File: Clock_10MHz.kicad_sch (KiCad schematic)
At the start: 8 parts, among them U3 74LV8154, U4 74LS151, X1 ASCO

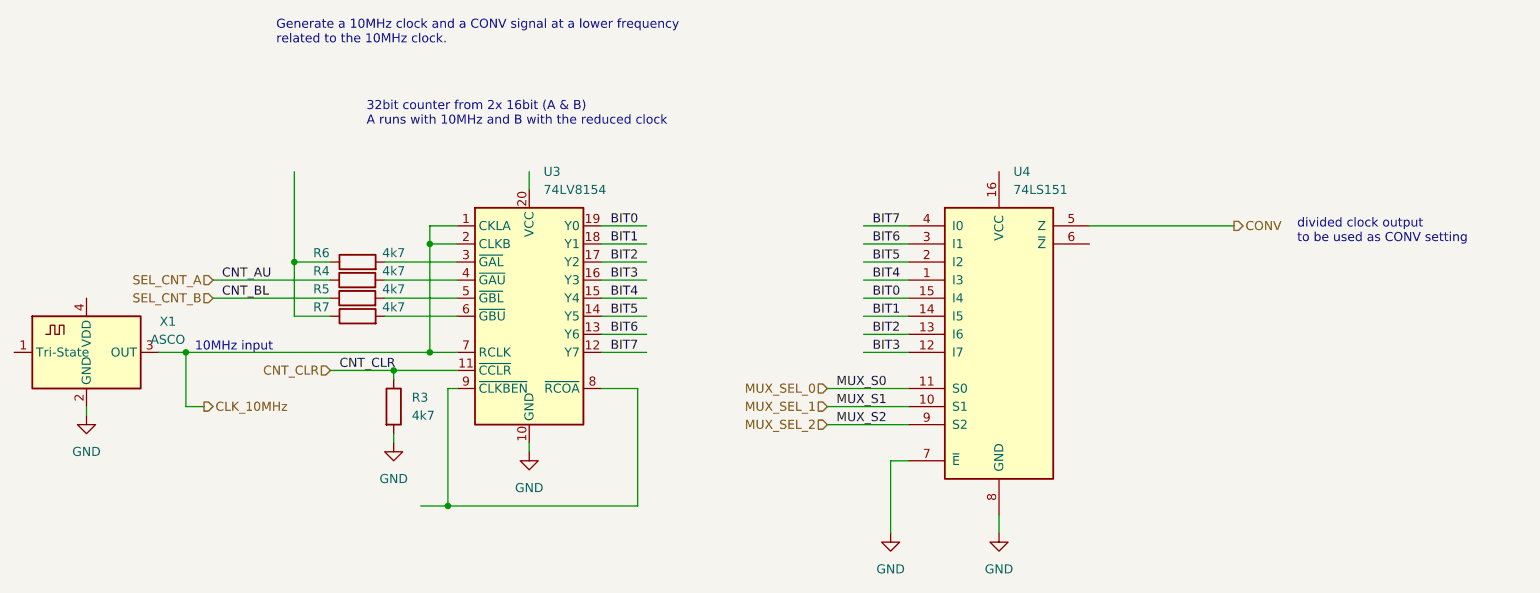
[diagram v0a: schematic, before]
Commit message: connected the ICs to 5V digital power
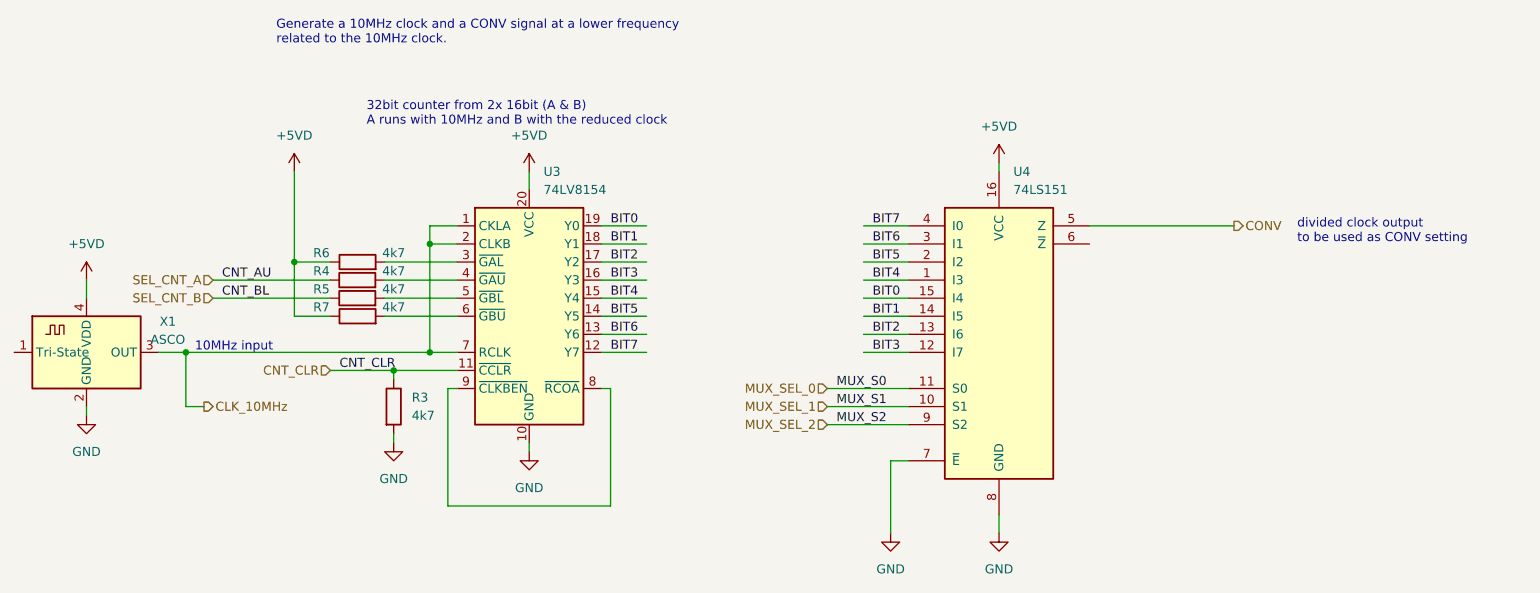
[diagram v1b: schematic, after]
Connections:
- net +5VD: now reaches R6.1, R7.1
- net +5VD: now also U3.20 (VCC), U4.16 (VCC), X1.4 (VDD)
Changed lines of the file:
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@@
   (junction (at 85.09 90.17) (diameter 0) (color 0 0 0 0)
   )
-  (junction (at 87.63 111.76) (diameter 0) (color 0 0 0 0)
-  )
   (junction (at 85.09 74.93) (diameter 0) (color 0 0 0 0)
   )
@@
     (stroke (width 0) (type default) (color 0 0 0 0))
   )
+  (wire (pts (xy 165.1 63.5) (xy 165.1 64.77))
+    (stroke (width 0) (type default) (color 0 0 0 0))
+  )
   (wire (pts (xy 85.09 74.93) (xy 88.9 74.93))
     (stroke (width 0) (type default) (color 0 0 0 0))
@@
     (stroke (width 0) (type default) (color 0 0 0 0))
   )
-  (wire (pts (xy 83.82 111.76) (xy 87.63 111.76))
-    (stroke (width 0) (type default) (color 0 0 0 0))
-  )
-  (wire (pts (xy 114.3 111.76) (xy 114.3 95.25))
+  (wire (pts (xy 110.49 111.76) (xy 110.49 95.25))
     (stroke (width 0) (type default) (color 0 0 0 0))
   )
@@
     (stroke (width 0) (type default) (color 0 0 0 0))
   )
-  (wire (pts (xy 109.22 95.25) (xy 114.3 95.25))
+  (wire (pts (xy 109.22 95.25) (xy 110.49 95.25))
     (stroke (width 0) (type default) (color 0 0 0 0))
   )
@@
     (stroke (width 0) (type default) (color 0 0 0 0))
   )
-  (wire (pts (xy 87.63 111.76) (xy 114.3 111.76))
+  (wire (pts (xy 87.63 111.76) (xy 110.49 111.76))
     (stroke (width 0) (type default) (color 0 0 0 0))
   )
@@
   )
   (wire (pts (xy 88.9 95.25) (xy 87.63 95.25))
+    (stroke (width 0) (type default) (color 0 0 0 0))
+  )
+  (wire (pts (xy 36.83 80.01) (xy 36.83 82.55))
     (stroke (width 0) (type default) (color 0 0 0 0))
   )
@@
     (pin "4")
   )
+  (symbol (lib_id "power:+5VD") (at 66.04 64.77 0) (unit 1)
+    (in_bom yes) (on_board yes) (fields_autoplaced)
+    (property "Reference" "#PWR?" (id 0) (at 66.04 68.58 0)
+      (effects (font (size 1.27 1.27)) hide)
+    )
+    (property "Value" "+5VD" (id 1) (at 66.04 59.69 0))
+    (property "Footprint" "" (id 2) (at 66.04 64.77 0)
+      (effects (font (size 1.27 1.27)) hide)
+    )
+    (property "Datasheet" "" (id 3) (at 66.04 64.77 0)
+      (effects (font (size 1.27 1.27)) hide)
+    )
+    (pin "1")
+  )
   (symbol (lib_id "74xx:74LS151") (at 165.1 87.63 0) (unit 1)
     (in_bom yes) (on_board yes) (fields_autoplaced)
@@
     (pin "2")
   )
+  (symbol (lib_id "power:+5VD") (at 36.83 80.01 0) (unit 1)
+    (in_bom yes) (on_board yes) (fields_autoplaced)
+    (property "Reference" "#PWR?" (id 0) (at 36.83 83.82 0)
+      (effects (font (size 1.27 1.27)) hide)
+    )
+    (property "Value" "+5VD" (id 1) (at 36.83 74.93 0))
+    (property "Footprint" "" (id 2) (at 36.83 80.01 0)
+      (effects (font (size 1.27 1.27)) hide)
+    )
+    (property "Datasheet" "" (id 3) (at 36.83 80.01 0)
+      (effects (font (size 1.27 1.27)) hide)
+    )
+    (pin "1")
+  )
   (symbol (lib_id "power:GND") (at 36.83 99.06 0) (unit 1)
     (in_bom yes) (on_board yes) (fields_autoplaced)
@@
       (effects (font (size 1.27 1.27)) hide)
     )
+    (pin "1")
+  )
+  (symbol (lib_id "power:+5VD") (at 165.1 63.5 0) (unit 1)
+    (in_bom yes) (on_board yes) (fields_autoplaced)
+    (property "Reference" "#PWR?" (id 0) (at 165.1 67.31 0)
+      (effects (font (size 1.27 1.27)) hide)
+    )
+    (property "Value" "+5VD" (id 1) (at 165.1 58.42 0))
+    (property "Footprint" "" (id 2) (at 165.1 63.5 0)
+      (effects (font (size 1.27 1.27)) hide)
+    )
+    (property "Datasheet" "" (id 3) (at 165.1 63.5 0)
+      (effects (font (size 1.27 1.27)) hide)
+    )
+    (pin "1")
+  )
+  (symbol (lib_id "power:+5VD") (at 99.06 64.77 0) (unit 1)
+    (in_bom yes) (on_board yes) (fields_autoplaced)
+    (property "Reference" "#PWR?" (id 0) (at 99.06 68.58 0)
+      (effects (font (size 1.27 1.27)) hide)
+    )
+    (property "Value" "+5VD" (id 1) (at 99.06 59.69 0))
+    (property "Footprint" "" (id 2) (at 99.06 64.77 0)
+      (effects (font (size 1.27 1.27)) hide)
+    )
+    (property "Datasheet" "" (id 3) (at 99.06 64.77 0)
+      (effects (font (size 1.27 1.27)) hide)
+    )
